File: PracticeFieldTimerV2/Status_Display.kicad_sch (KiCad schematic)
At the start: 4 parts, among them U2 PCF8574N, U3 20 x 4 LCD

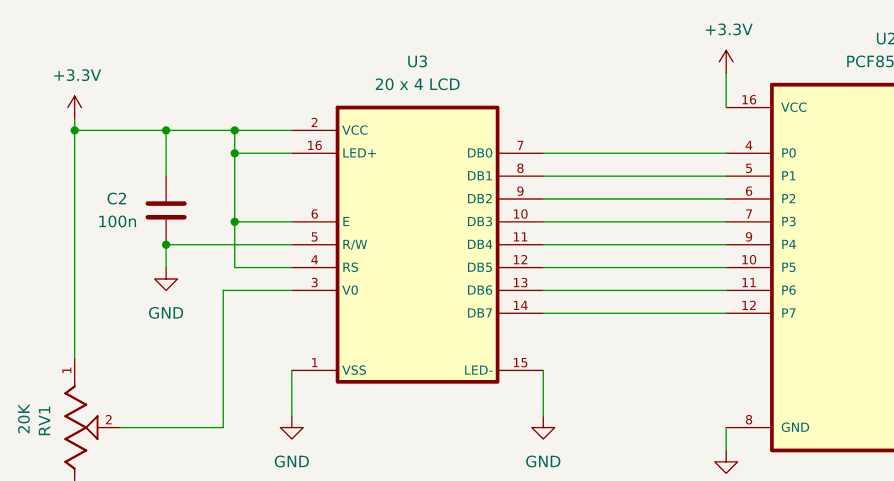
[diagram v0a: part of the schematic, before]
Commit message: Fix egregious wiring error in the LCD Display
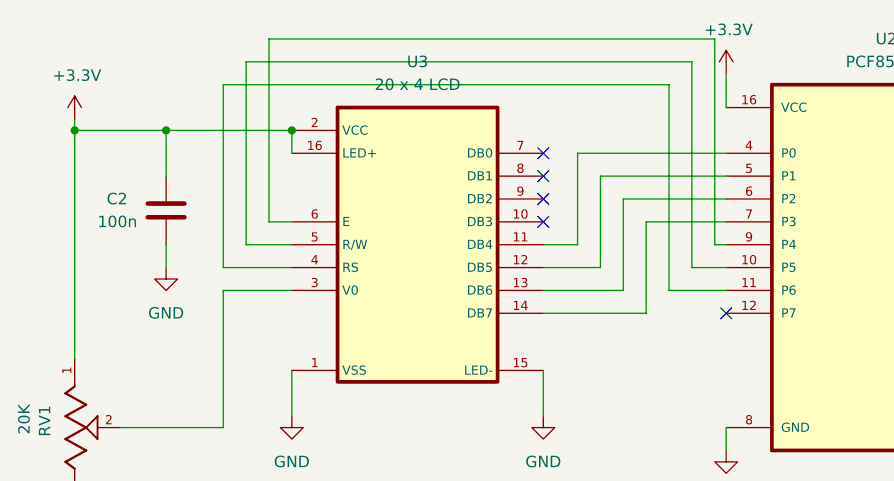
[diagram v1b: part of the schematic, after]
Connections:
- net +3.3V: no longer U3.4 (RS), U3.6 (E)
- net GND: no longer U3.5 (R/W)
- net at U3.10 (DB3): no longer U2.7 (P3)
- net at U3.11 (DB4): now also U2.4 (P0); no longer U2.9 (P4)
- net at U3.12 (DB5): now also U2.5 (P1); no longer U2.10 (P5)
- net at U3.13 (DB6): now also U2.6 (P2); no longer U2.11 (P6)
- net at U3.14 (DB7): now also U2.7 (P3); no longer U2.12 (P7)
- net at U3.7 (DB0): no longer U2.4 (P0)
- net at U3.8 (DB1): no longer U2.5 (P1)
- net at U3.9 (DB2): no longer U2.6 (P2)
- new net: U2.11 (P6), U3.4 (RS)
- new net: U2.10 (P5), U3.5 (R/W)
- new net: U2.9 (P4), U3.6 (E)
- no-connect marks 1 -> 6

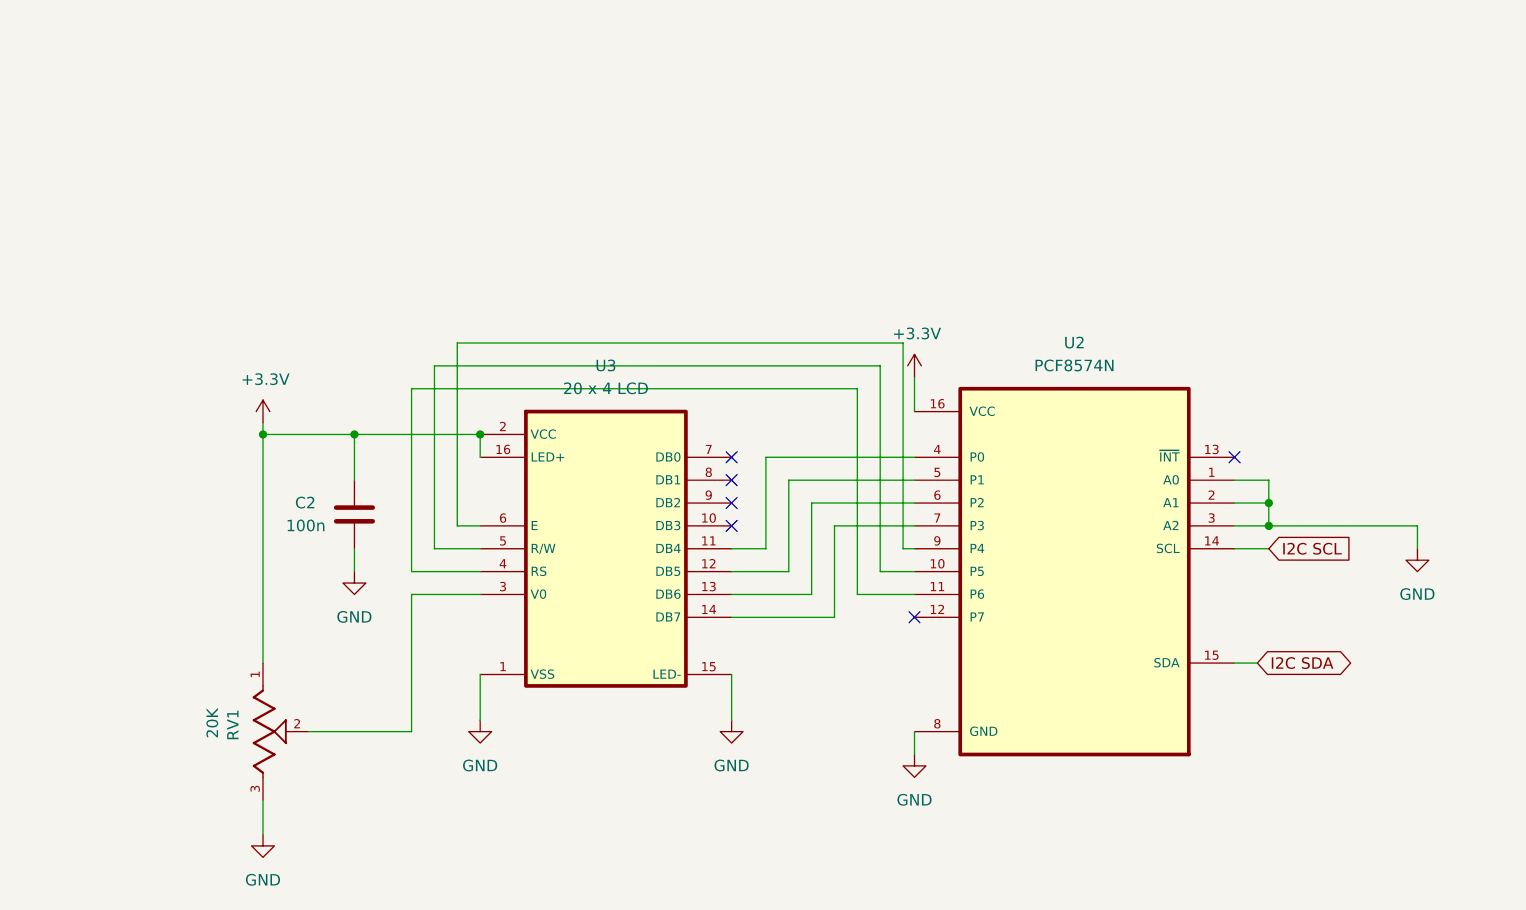
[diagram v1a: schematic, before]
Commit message: Fix reversed power and ground on LCD backlight LED.
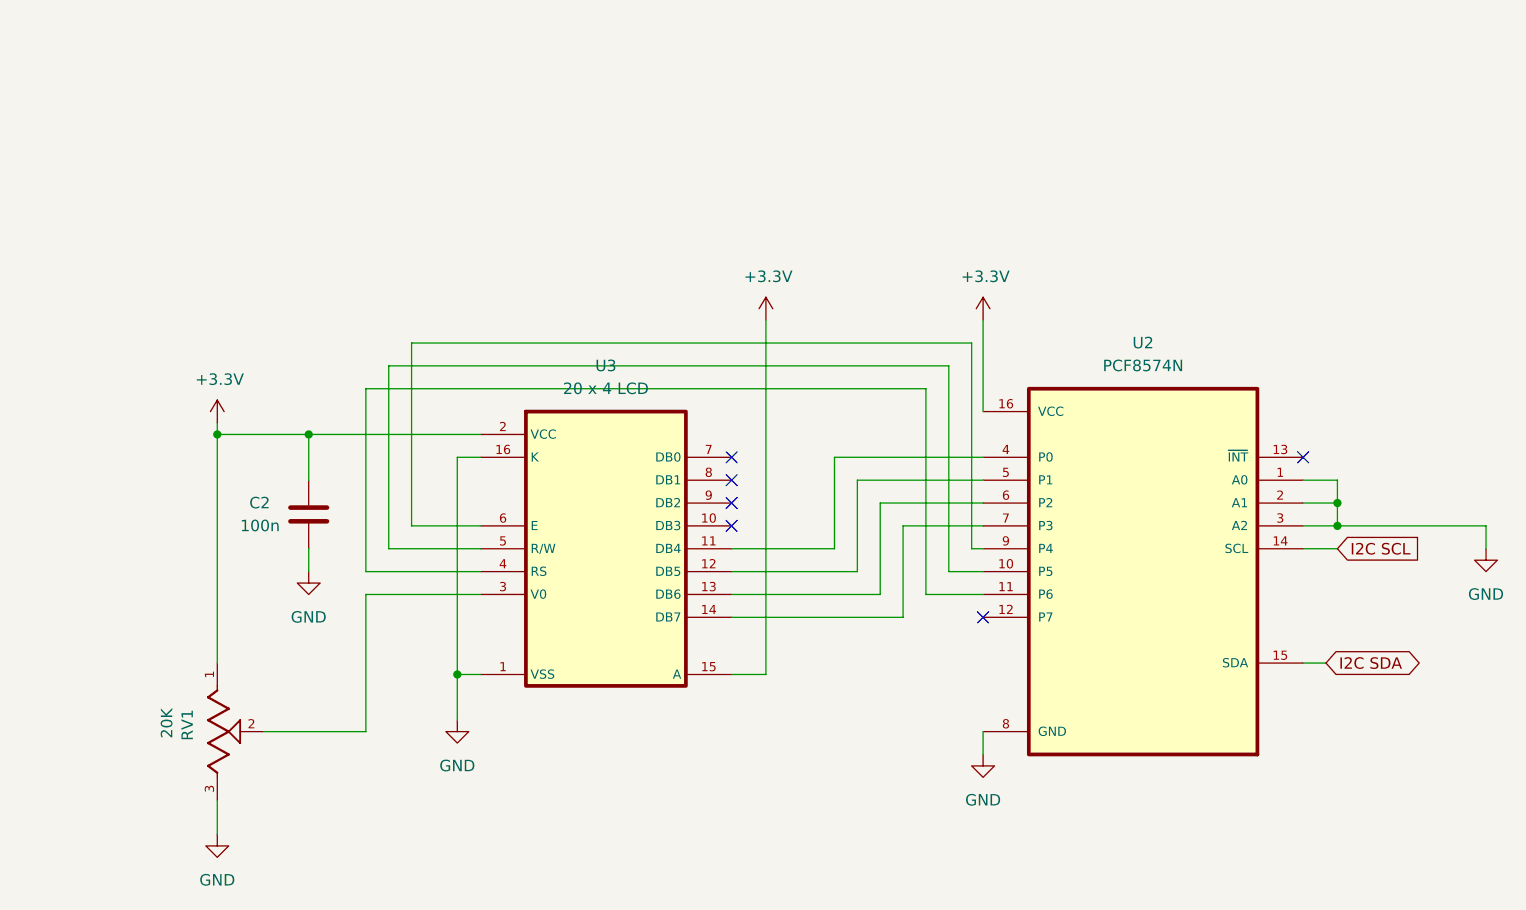
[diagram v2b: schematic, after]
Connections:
- net +3.3V: now also U3.15 (A); no longer U3.16 (LED+)
- net GND: now also U3.16 (K); no longer U3.15 (LED-)
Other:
- moved on the sheet: C2, RV1, U2

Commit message: Power the LCD backlight from +5 to minimize load on the ESP32 voltage reducer and for maximum brightness.
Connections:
- net +3.3V: no longer U3.15 (A)
- new net +5V: U3.15 (A)
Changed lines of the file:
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@@
+	)
+	(symbol
+		(lib_id "power:+5V")
+		(at 154.94 69.85 0)
+		(unit 1)
+		(exclude_from_sim no)
+		(in_bom yes)
+		(on_board yes)
+		(dnp no)
+		(property "Reference" "#PWR024"
+			(at 154.94 73.66 0)
+			(effects
+				(font
+					(size 1.27 1.27)
+				)
+				(hide yes)
+			)
+		)
+		(property "Value" "+5V"
+			(at 157.988 68.072 0)
+			(effects
+				(font
+					(size 1.27 1.27)
+				)
+			)
+		)
+		(property "Footprint" ""
+			(at 154.94 69.85 0)
+			(effects
+				(font
+					(size 1.27 1.27)
+				)
+				(hide yes)
+			)
+		)
+		(property "Datasheet" ""
+			(at 154.94 69.85 0)
+			(effects
+				(font
+					(size 1.27 1.27)
+				)
+				(hide yes)
+			)
+		)
+		(property "Description" "Power symbol creates a global label with name \"+5V\""
+			(at 154.94 69.85 0)
+			(effects
+				(font
+					(size 1.27 1.27)
+				)
+				(hide yes)
+			)
+		)
+		(pin "1"
+		)
+		(instances
+			(project "PracticeFieldTimerV2"
+				(path "/a82ebad5-0442-461b-8944-6652da9a0796/03113a51-d978-4e2f-a8a7-ba137b470bd3"
+					(reference "#PWR024")
+					(unit 1)
+				)
+			)
+		)
 	)
 	(symbol
@@
 					(unit 1)
 				)
-			)
-		)
-	)
-	(symbol
-		(lib_id "power:+3.3V")
-		(at 154.94 69.85 0)
-		(mirror y)
-		(unit 1)
-		(exclude_from_sim no)
-		(in_bom yes)
-		(on_board yes)
-		(dnp no)
-		(property "Reference" "#PWR024"
-			(at 154.94 73.66 0)
-			(effects
-				(font
-					(size 1.27 1.27)
-				)
-				(hide yes)
-			)
-		)
-		(property "Value" "+3.3V"
-			(at 155.194 65.024 0)
-			(effects
-				(font
-					(size 1.27 1.27)
-				)
-			)
-		)
-		(property "Footprint" ""
-			(at 154.94 69.85 0)
-			(effects
-				(font
-					(size 1.27 1.27)
-				)
-				(hide yes)
-			)
-		)
-		(property "Datasheet" ""
-			(at 154.94 69.85 0)
-			(effects
-				(font
-					(size 1.27 1.27)
-				)
-				(hide yes)
-			)
-		)
-		(property "Description" "Power symbol creates a global label with name \"+3.3V\""
-			(at 154.94 69.85 0)
-			(effects
-				(font
-					(size 1.27 1.27)
-				)
-				(hide yes)
-			)
-		)
-		(pin "1"
-		)
-		(instances
-			(project "PracticeFieldTimerV2"
-				(path "/a82ebad5-0442-461b-8944-6652da9a0796/03113a51-d978-4e2f-a8a7-ba137b470bd3"
-					(reference "#PWR024")
-					(unit 1)
-				)

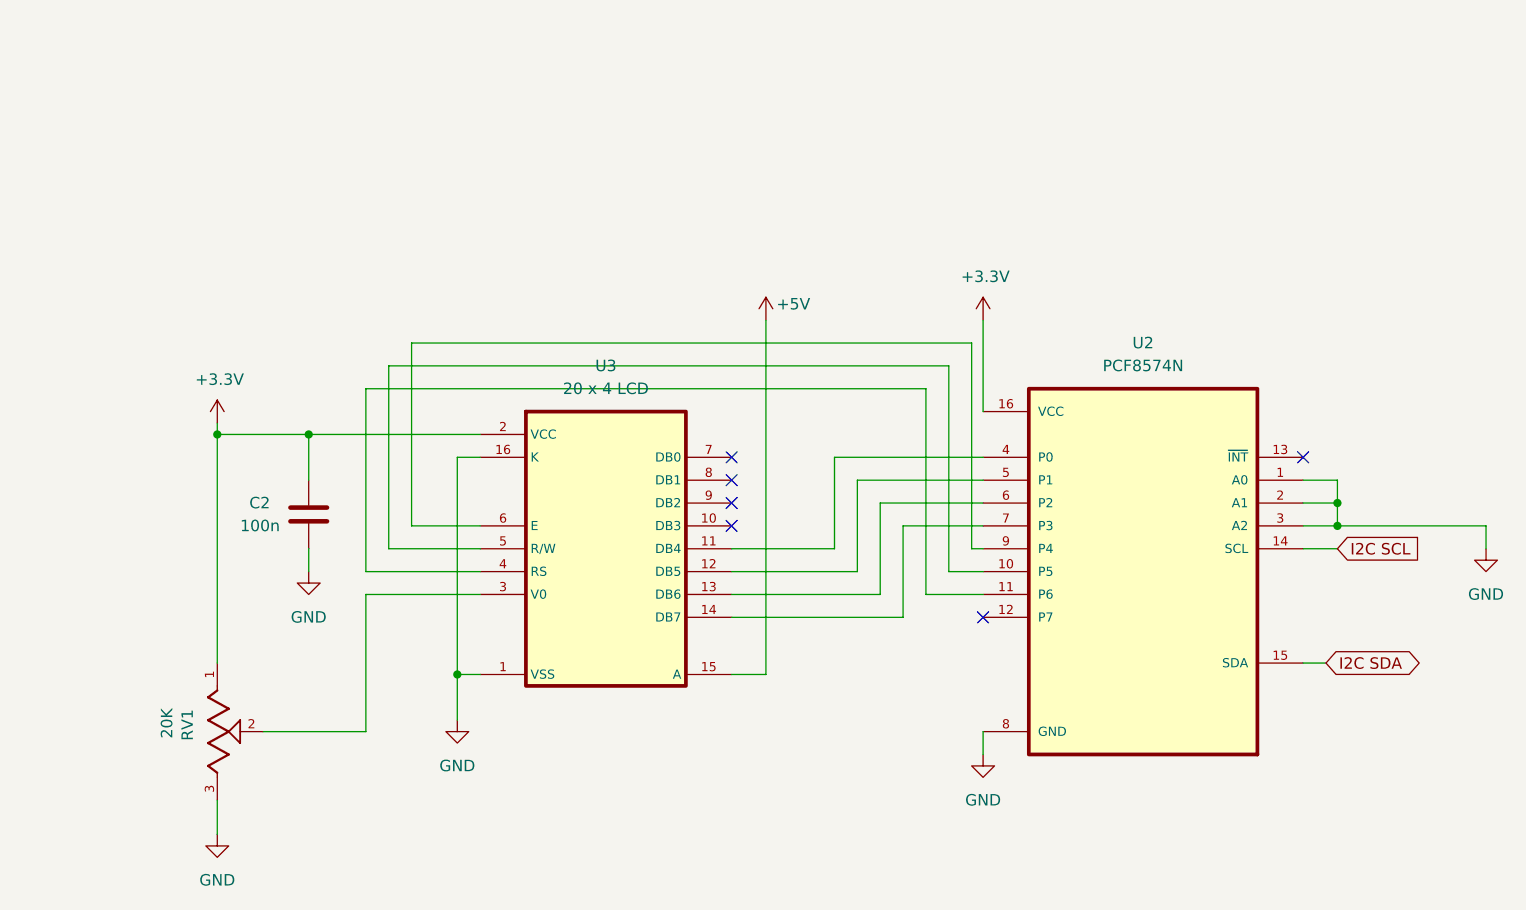
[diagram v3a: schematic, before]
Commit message: Remove on-board LCD Module and I2C->parallel byte converter. Add terminal strip for off-board display. Shrink the board. The board is still a bit spread out, but the changes are significant enough to commit.
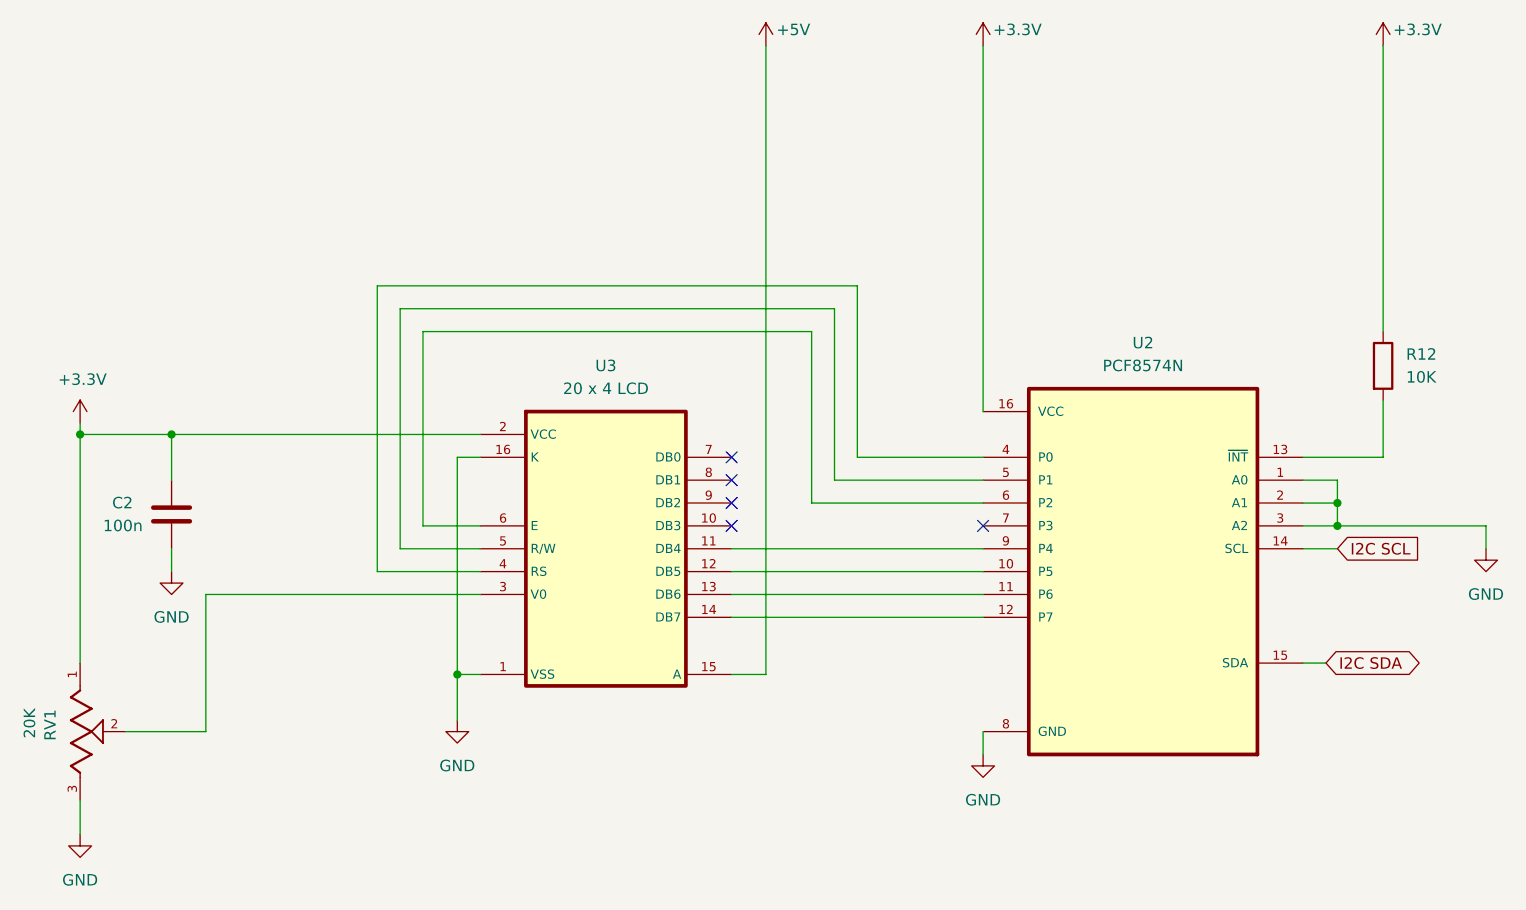
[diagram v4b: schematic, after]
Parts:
- added R12: 10K, Resistor_THT:R_Axial_DIN0207_L6.3mm_D2.5mm_P15.24mm_Horizontal, symbol Device:R
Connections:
- net +3.3V: now also R12.1
- net at U3.11 (DB4): now also U2.9 (P4); no longer U2.4 (P0)
- net at U3.12 (DB5): now also U2.10 (P5); no longer U2.5 (P1)
- net at U3.13 (DB6): now also U2.11 (P6); no longer U2.6 (P2)
- net at U3.14 (DB7): now also U2.12 (P7); no longer U2.7 (P3)
- net at U3.4 (RS): now also U2.4 (P0); no longer U2.11 (P6)
- net at U3.5 (R/W): now also U2.5 (P1); no longer U2.10 (P5)
- net at U3.6 (E): now also U2.6 (P2); no longer U2.9 (P4)
- net at U2.13 (~{INT}): now also R12.2
- no-connect marks 6 -> 5
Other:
- moved on the sheet: C2, RV1
